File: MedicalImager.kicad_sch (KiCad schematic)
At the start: 0 parts

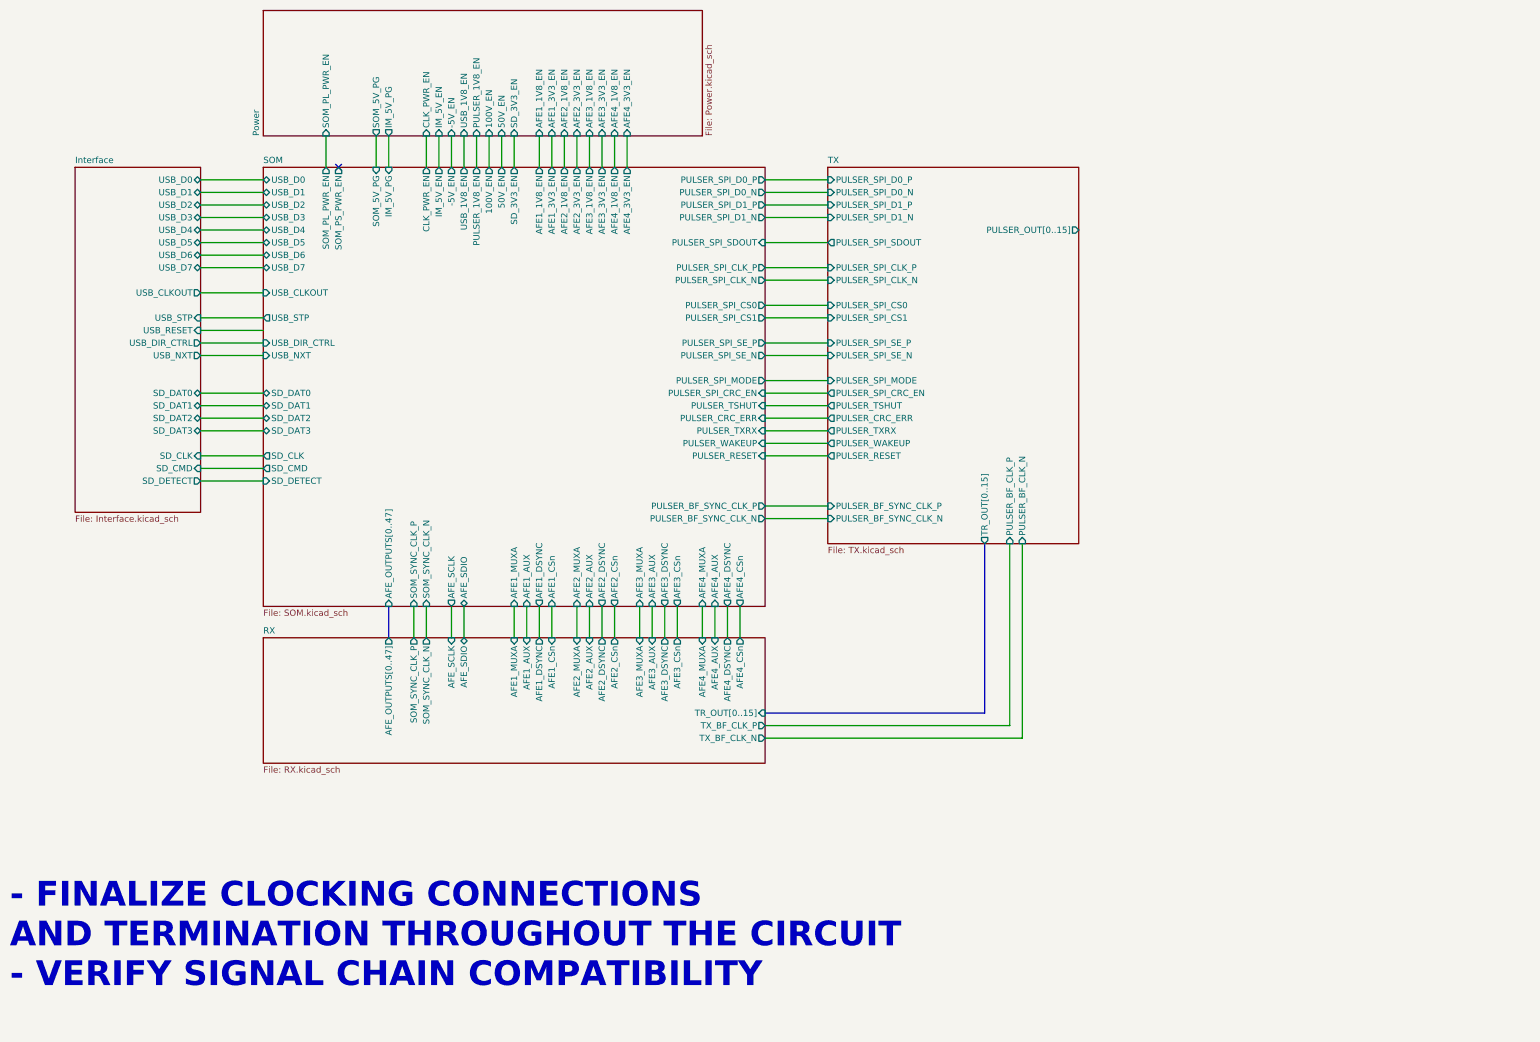
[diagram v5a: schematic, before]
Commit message: HDMI was requested so add it and give the signal chain a final revision
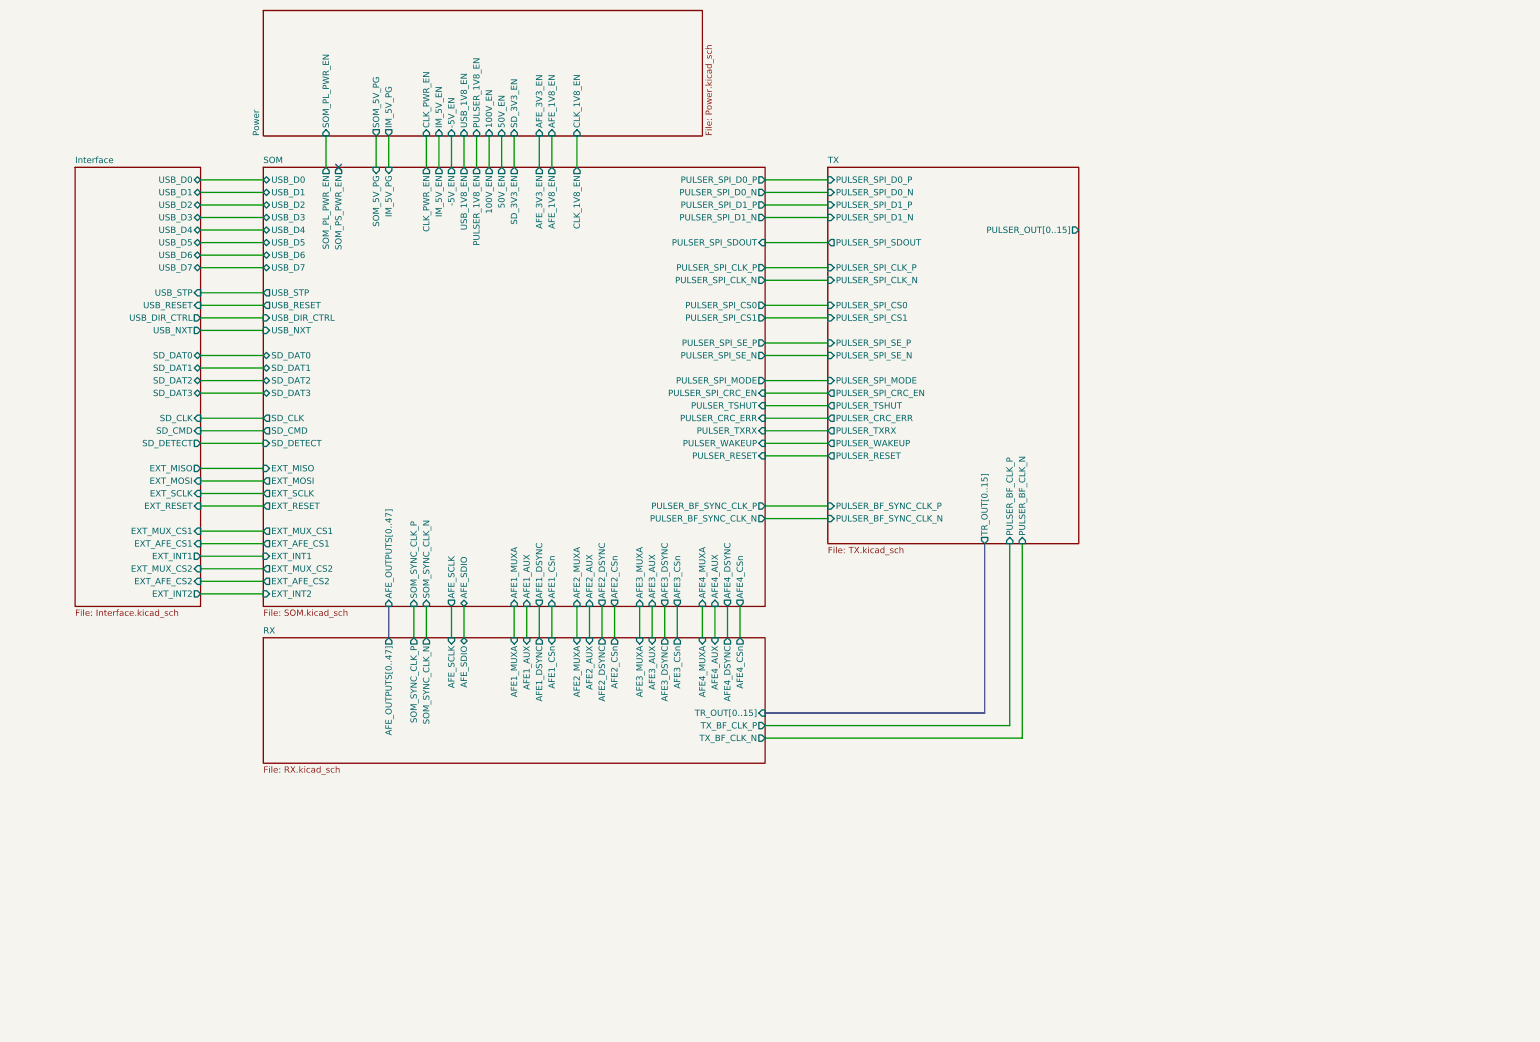
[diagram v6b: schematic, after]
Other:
- sheet Interface ports: added EXT_AFE_CS1, EXT_AFE_CS2, EXT_INT1, EXT_INT2, EXT_MISO, EXT_MOSI, EXT_MUX_CS1, EXT_MUX_CS2, EXT_RESET, EXT_SCLK; removed USB_CLKOUT
- sheet Power ports: added AFE_1V8_EN, AFE_3V3_EN, CLK_1V8_EN; removed AFE1_1V8_EN, AFE1_3V3_EN, AFE2_1V8_EN, AFE2_3V3_EN, AFE3_1V8_EN, AFE3_3V3_EN, AFE4_1V8_EN, AFE4_3V3_EN
- sheet SOM ports: added AFE_1V8_EN, AFE_3V3_EN, CLK_1V8_EN, EXT_AFE_CS1, EXT_AFE_CS2, EXT_INT1, EXT_INT2, EXT_MISO, EXT_MOSI, EXT_MUX_CS1, EXT_MUX_CS2, EXT_RESET, EXT_SCLK, USB_RESET; removed AFE1_1V8_EN, AFE1_3V3_EN, AFE2_1V8_EN, AFE2_3V3_EN, AFE3_1V8_EN, AFE3_3V3_EN, AFE4_1V8_EN, AFE4_3V3_EN, USB_CLKOUT
- note removed: "- FINALIZE CLOCKING CONNECTIONS AND TERMINATION THROUGHOUT THE CIRCUIT - VERIFY SIGNAL CHAIN COMPATIBILITY"

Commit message: ALL IS DONE EXCEPT HDMI PLEASE HELP
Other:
- sheet Interface ports: added USB_26MHZ; removed none
- sheet SOM ports: added USB_26MHZ; removed none

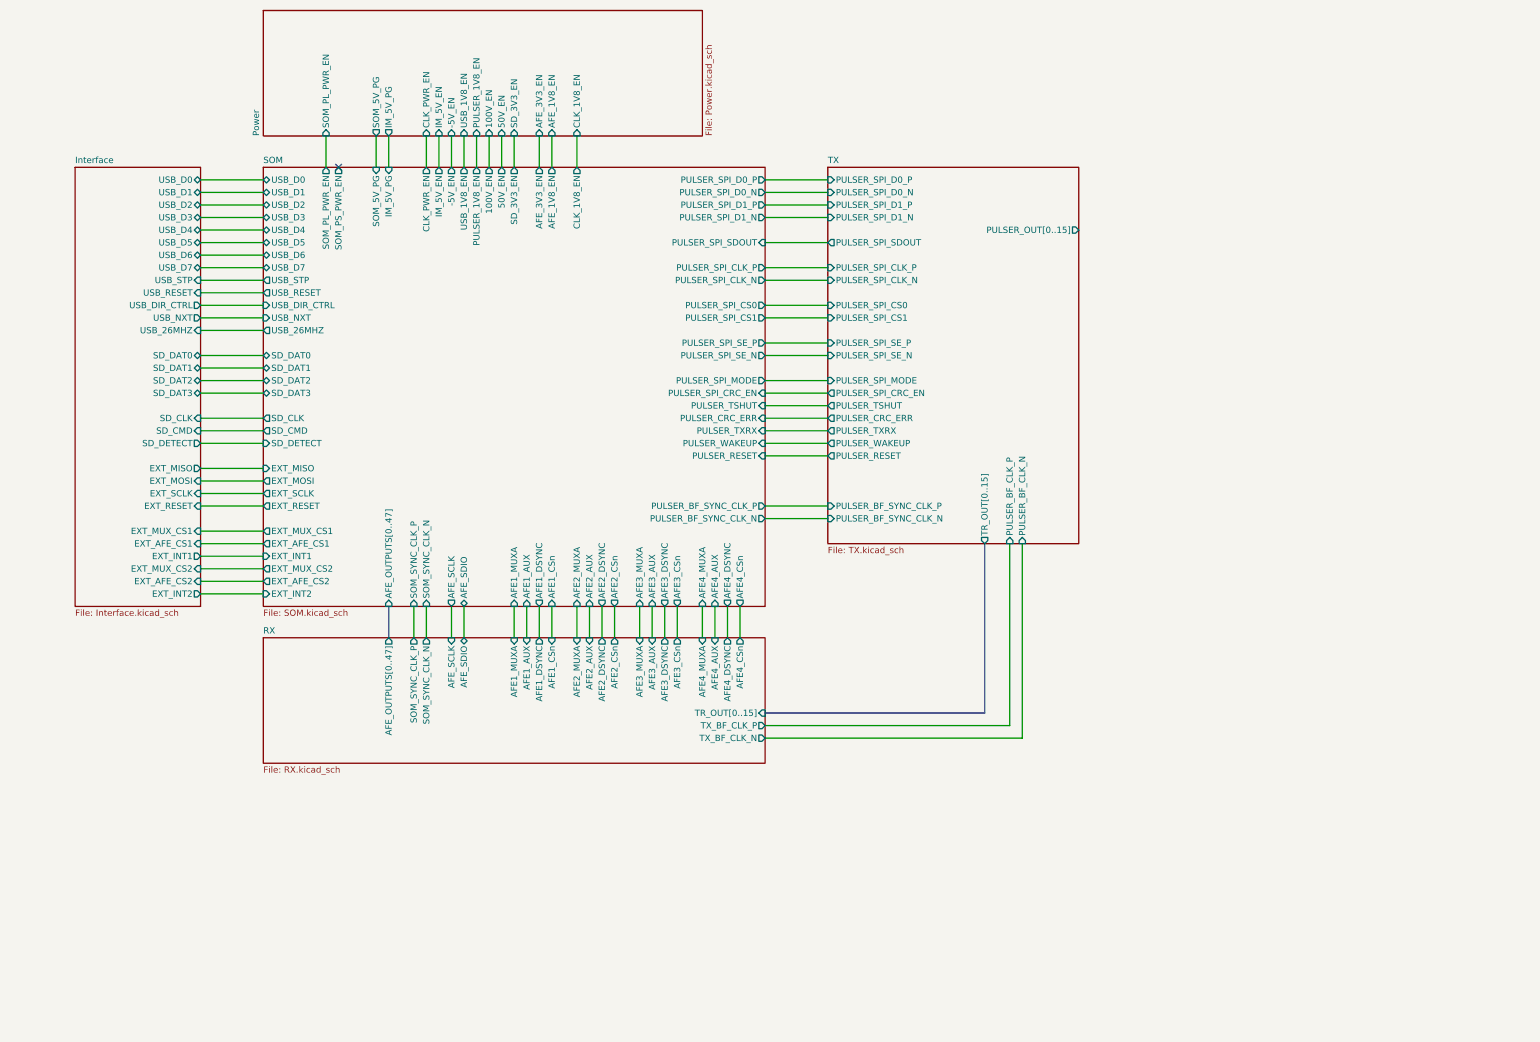
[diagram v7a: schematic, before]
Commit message: started layout, finished 90% of individual section placement, need to finish remaining and integrate together in PCB and apply schematic edits before
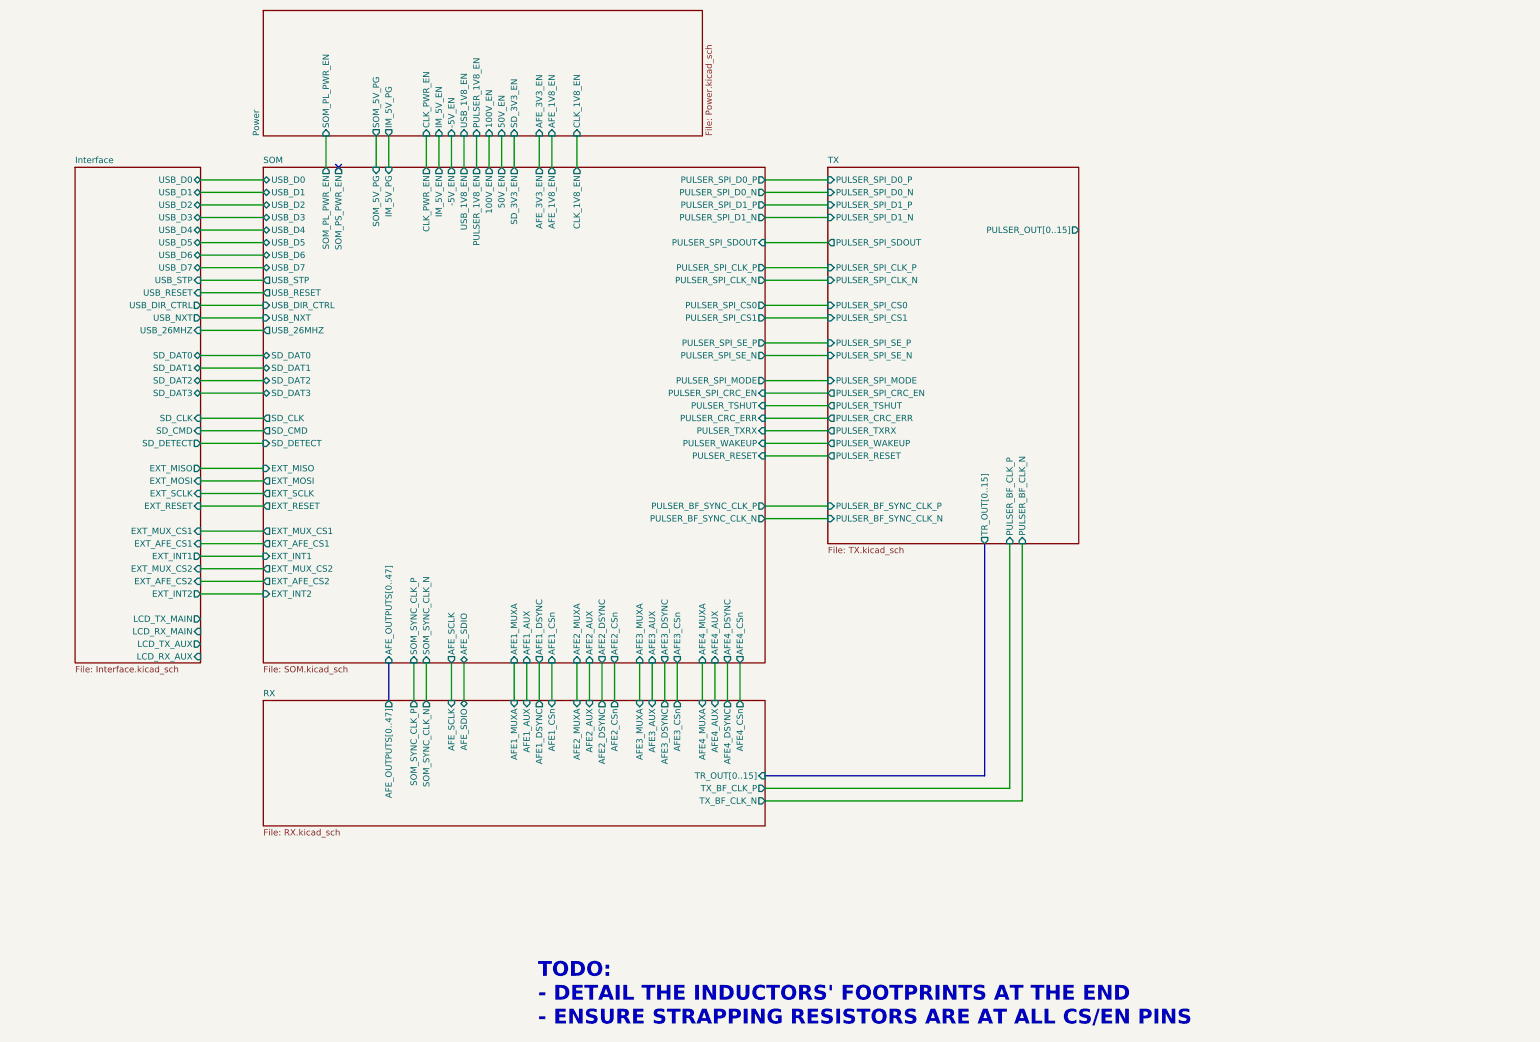
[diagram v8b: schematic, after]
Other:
- sheet Interface ports: added LCD_RX_AUX, LCD_RX_MAIN, LCD_TX_AUX, LCD_TX_MAIN; removed none
- note added: "TODO: - DETAIL THE INDUCTORS' FOOTPRINTS AT THE END - ENSURE STRAPPING RESISTORS ARE AT ALL CS/EN PINS"
